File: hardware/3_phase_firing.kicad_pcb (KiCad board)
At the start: 2 copper layers, 90 x 50 mm, 32 parts, among them J1 PHASE_IN_1, J2 PHASE_OUT_1, J3 PHASE_IN_2, J4 PHASE_OUT_2, Q1 BT136-500, Q2 BT136-500, Q3 BT136-500, U1 4N25, U2 4N25, U3 4N25, U4 MEGA_PRO_EMBED_CH340G_{slash}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, U5 MOC3012M, U6 MOC3012M, U7 MOC3012M

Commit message: pcb done
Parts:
- added G***: LOGO, logo_uny:logo_uny_15mm, F.Cu at (153.0, 84.0)
- added REF**: MountingHole_2.5mm_Pad, MountingHole:MountingHole_2.5mm_Pad, F.Cu at (82.0, 125.0)
- added REF**: MountingHole_2.5mm_Pad, MountingHole:MountingHole_2.5mm_Pad, F.Cu at (212.0, 125.0)
- added REF**: MountingHole_2.5mm_Pad, MountingHole:MountingHole_2.5mm_Pad, F.Cu at (212.0, 75.0)
- added REF**: MountingHole_2.5mm_Pad, MountingHole:MountingHole_2.5mm_Pad, F.Cu at (82.0, 75.0)
- U1, U2, U3, U5, U6, U7: footprint Package_DIP:DIP-6_W7.62mm -> Package_DIP:DIP-6_W8.89mm_SMDSocket_LongPads
- U4: moved to B.Cu
- moved U4 155.5 mm to (152.3, 99.0), turned to -90 degrees
- moved R5 106.8 mm to (111.0, 109.0)
- moved R6 106.2 mm to (111.0, 115.0)
- moved U3 79.6 mm to (124.0, 114.3)
- moved J1 67.0 mm to (85.0, 89.9)
- moved J3 67.0 mm to (85.0, 100.5)
- moved R3 58.0 mm to (111.0, 96.0)
- moved R8 56.5 mm to (176.0, 92.0)
- moved U2 54.3 mm to (124.0, 99.0)
- moved Q3 53.6 mm to (200.0, 80.5), turned to -90 degrees
- moved Q2 50.9 mm to (200.0, 96.5), turned to -90 degrees
- moved R7 46.5 mm to (176.0, 77.0)
- moved R15 45.0 mm to (193.0, 87.0)
- moved J2 43.6 mm to (211.0, 106.5)
- moved J4 43.6 mm to (211.0, 95.9)
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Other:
- board size 90 x 50 mm -> 140 x 60 mm
- board text added: "2022 (C) JPTE HFEAA"
- board text added: "MODUL ELDA PEMICU 3 FASA"

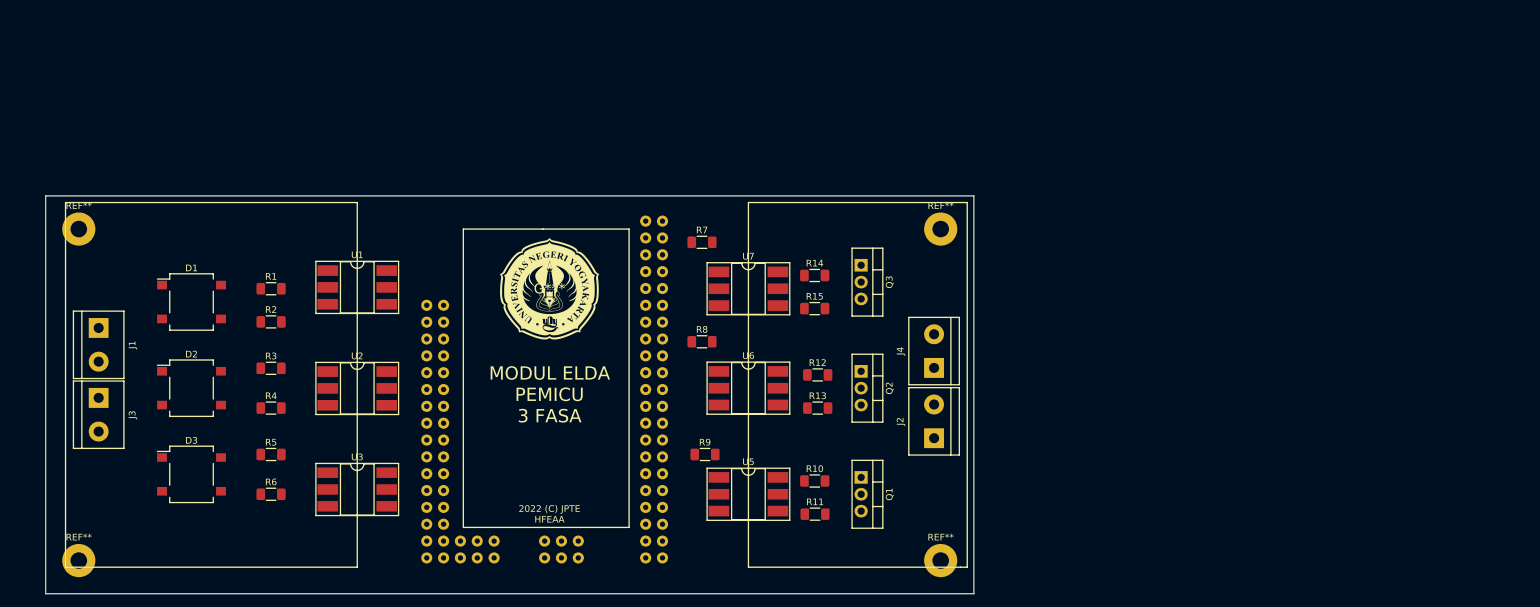
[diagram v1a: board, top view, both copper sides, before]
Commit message: modifying footprint
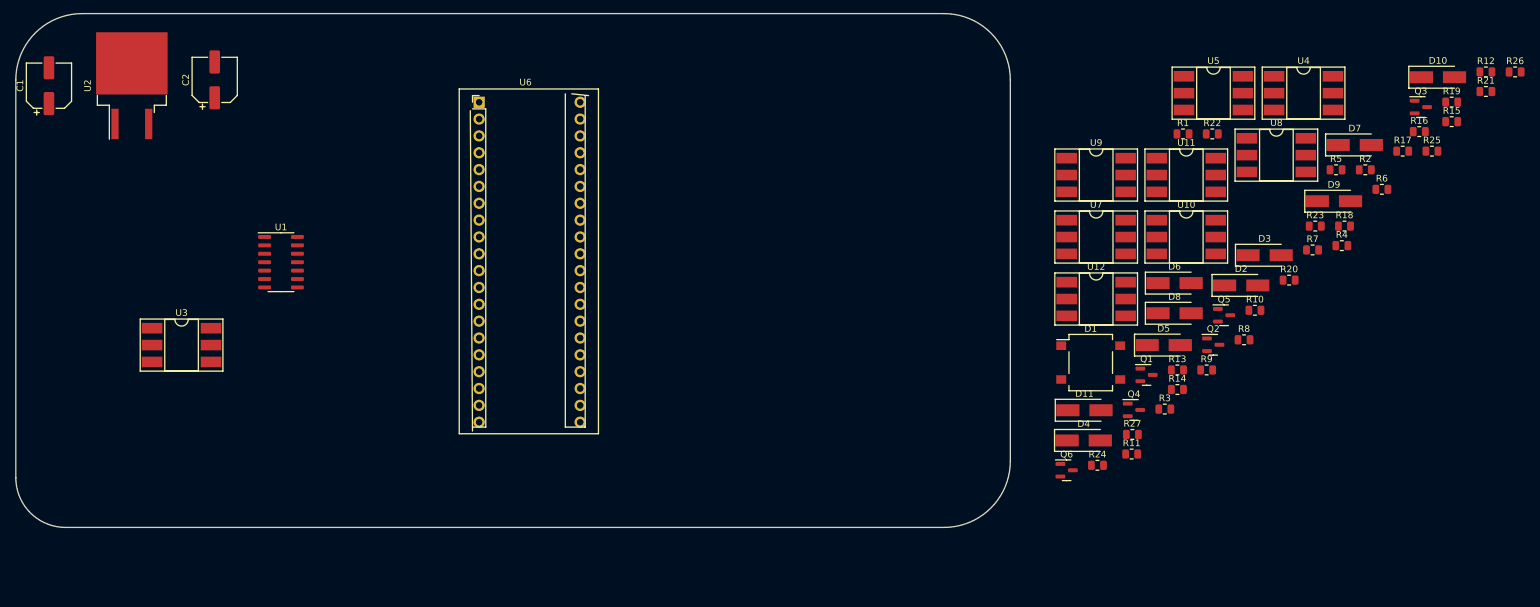
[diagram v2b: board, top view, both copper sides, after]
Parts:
- removed G***: LOGO, logo_uny:logo_uny_15mm
- removed J1: PHASE_IN_1, TerminalBlock:TerminalBlock_bornier-2_P5.08mm
- removed J2: PHASE_OUT_1, TerminalBlock:TerminalBlock_bornier-2_P5.08mm
- removed J3: PHASE_IN_2, TerminalBlock:TerminalBlock_bornier-2_P5.08mm
- removed J4: PHASE_OUT_2, TerminalBlock:TerminalBlock_bornier-2_P5.08mm
- removed REF** (x4): MountingHole_2.5mm_Pad, MountingHole:MountingHole_2.5mm_Pad
- added C1: 100uF, Capacitor_SMD:CP_Elec_6.3x7.7, F.Cu at (77.5, 53.4)
- added C2: 100uF, Capacitor_SMD:CP_Elec_6.3x7.7, F.Cu at (102.5, 52.5)
- added D10: 1N4007, Diode_SMD:D_SMA_Handsoldering, F.Cu at (287.0, 52.1)
- added D11: 1N4007, Diode_SMD:D_SMA_Handsoldering, F.Cu at (233.7, 102.3)
- added D4: 1N4007, Diode_SMD:D_SMA_Handsoldering, F.Cu at (233.6, 106.9)
- added D5: 1N4007, Diode_SMD:D_SMA_Handsoldering, F.Cu at (245.6, 92.5)
- added D6: 1N4007, Diode_SMD:D_SMA_Handsoldering, F.Cu at (247.3, 83.2)
- added D7: 1N4007, Diode_SMD:D_SMA_Handsoldering, F.Cu at (274.4, 62.3)
- added D8: 1N4007, Diode_SMD:D_SMA_Handsoldering, F.Cu at (247.3, 87.7)
- added D9: 1N4007, Diode_SMD:D_SMA_Handsoldering, F.Cu at (271.3, 70.8)
- added Q4: MMBT3904, Package_TO_SOT_SMD:SOT-23, F.Cu at (241.2, 102.3)
- added Q5: MMBT3904, Package_TO_SOT_SMD:SOT-23, F.Cu at (254.7, 88.0)
- added Q6: MMBT3904, Package_TO_SOT_SMD:SOT-23, F.Cu at (231.0, 111.4)
- added R16: 2K2, Resistor_SMD:R_0805_2012Metric, F.Cu at (284.2, 60.3)
- added R17: 2K2, Resistor_SMD:R_0805_2012Metric, F.Cu at (281.7, 63.2)
- added R18: 2K2, Resistor_SMD:R_0805_2012Metric, F.Cu at (272.9, 74.5)
- added R19: 10K, Resistor_SMD:R_0805_2012Metric, F.Cu at (289.1, 55.9)
- added R20: 10K, Resistor_SMD:R_0805_2012Metric, F.Cu at (264.6, 82.7)
- added R21: 10K, Resistor_SMD:R_0805_2012Metric, F.Cu at (294.2, 54.2)
- added R22: 2K2, Resistor_SMD:R_0805_2012Metric, F.Cu at (253.0, 60.6)
- added R23: 2K2, Resistor_SMD:R_0805_2012Metric, F.Cu at (268.5, 74.5)
- added R24: 2K2, Resistor_SMD:R_0805_2012Metric, F.Cu at (235.6, 110.6)
- added R25: 2K2, Resistor_SMD:R_0805_2012Metric, F.Cu at (286.1, 63.2)
- added R26: 2K2, Resistor_SMD:R_0805_2012Metric, F.Cu at (298.6, 51.3)
- added R27: 2K2, Resistor_SMD:R_0805_2012Metric, F.Cu at (240.9, 106.0)
- added U10: 4N35, Package_DIP:DIP-6_W8.89mm_SMDSocket_LongPads, F.Cu at (249.0, 76.2)
- added U11: 4N35, Package_DIP:DIP-6_W8.89mm_SMDSocket_LongPads, F.Cu at (249.0, 66.8)
- added U12: 4N35, Package_DIP:DIP-6_W8.89mm_SMDSocket_LongPads, F.Cu at (235.4, 85.5)
- added U8: 4N35, Package_DIP:DIP-6_W8.89mm_SMDSocket_LongPads, F.Cu at (262.6, 63.9)
- added U9: 4N35, Package_DIP:DIP-6_W8.89mm_SMDSocket_LongPads, F.Cu at (235.4, 66.8)
- D2, D3: value DB106S -> 1N4007; footprint Diode_SMD:Diode_Bridge_OnSemi_SDIP-4L -> Diode_SMD:D_SMA_Handsoldering
- Q1, Q2, Q3: value BT136-500 -> MMBT3904; footprint Package_TO_SOT_THT:TO-220-3_Vertical -> Package_TO_SOT_SMD:SOT-23
- R1, R2, R3, R4, R5, R6: value 2K2 -> 10K; footprint Resistor_SMD:R_1206_3216Metric_Pad1.30x1.75mm_HandSolder -> Resistor_SMD:R_0805_2012Metric
- R10, R12, R13, R14, R15: value 330 -> 10K; footprint Resistor_SMD:R_1206_3216Metric_Pad1.30x1.75mm_HandSolder -> Resistor_SMD:R_0805_2012Metric
- R11: value 330 -> 100K; footprint Resistor_SMD:R_1206_3216Metric_Pad1.30x1.75mm_HandSolder -> Resistor_SMD:R_0805_2012Metric
- R7, R9: value 10K -> 100K; footprint Resistor_SMD:R_1206_3216Metric_Pad1.30x1.75mm_HandSolder -> Resistor_SMD:R_0805_2012Metric
- R8: footprint Resistor_SMD:R_1206_3216Metric_Pad1.30x1.75mm_HandSolder -> Resistor_SMD:R_0805_2012Metric
- U1: value 4N25 -> LM339; footprint Package_DIP:DIP-6_W8.89mm_SMDSocket_LongPads -> Package_SO:SOIC-14_3.9x8.7mm_P1.27mm
- U2: value 4N25 -> L7812; footprint Package_DIP:DIP-6_W8.89mm_SMDSocket_LongPads -> Package_TO_SOT_SMD:TO-263-2
- U3: value 4N25 -> 4N35
- U4: value MEGA_PRO_EMBED_CH340G_/_ATMEGA2560 -> 4N35; footprint MEGA_PRO_EMBED_CH340G___ATMEGA2560:MODULE_MEGA_PRO_EMBED_CH340G___ATMEGA2560 -> Package_DIP:DIP-6_W8.89mm_SMDSocket_LongPads; moved to F.Cu
- U5, U7: value MOC3012M -> 4N35
- U6: value MOC3012M -> YAAJ_WeAct_BlackPill_Part_Like; footprint Package_DIP:DIP-6_W8.89mm_SMDSocket_LongPads -> Footprints:YAAJ_WeAct_BlackPill_2
- moved R6 173.7 mm to (278.5, 69.0)
- moved R2 166.6 mm to (276.0, 66.1)
- moved R5 166.3 mm to (271.6, 66.1)
- moved D3 165.2 mm to (260.9, 79.0)
- moved R4 163.3 mm to (272.5, 77.5)
- moved D2 159.1 mm to (257.3, 83.5)
- moved R1 139.5 mm to (248.6, 60.6)
- moved D1 135.9 mm to (234.6, 95.1)
- moved R3 134.9 mm to (245.8, 102.2)
- moved U4 122.8 mm to (266.7, 54.5), turned to 0 degrees
- moved R12 110.7 mm to (294.2, 51.3)
- moved R15 100.1 mm to (289.1, 58.8)
- moved U5 92.6 mm to (253.1, 54.5)
- moved R7 92.1 mm to (268.1, 78.2)
- moved Q3 87.7 mm to (284.4, 56.6), turned to 0 degrees
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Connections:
- D1 pad 1: Net-(D1-Pad1) -> GNDS
- D1 pad 2: N -> PHASE_A
- D1 pad 4: PHASE_A -> NEUT
- D2 pad 2: N -> PHASE_A
- D3 pad 2: N -> PHASE_B
- Q1 pad 1: OUT_A -> TRIAC_MODE
- Q1 pad 2: PHASE_A -> Net-(Q1-Pad2)
- Q2 pad 1: OUT_B -> TRIAC_MODE
- Q2 pad 2: PHASE_B -> Net-(Q2-Pad2)
- Q3 pad 1: OUT_C -> TRIAC_MODE
- Q3 pad 2: PHASE_C -> Net-(Q3-Pad2)
- R1 pad 1: Net-(D1-Pad1) -> Net-(R1-Pad1)
- R1 pad 2: Net-(R1-Pad2) -> Net-(D2-Pad1)
- R10 pad 1: Net-(R10-Pad1) -> GNDS
- R10 pad 2: PHASE_A -> Net-(R10-Pad2)
- R11 pad 2: Net-(Q1-Pad3) -> VCC
- R12 pad 1: Net-(R12-Pad1) -> GNDS
- R12 pad 2: PHASE_B -> Net-(R11-Pad1)
- R13 pad 2: Net-(Q2-Pad3) -> VCC
- R14 pad 2: PHASE_C -> VCC
- R15 pad 2: Net-(Q3-Pad3) -> VCC
- R2 pad 1: Net-(D1-Pad3) -> GNDS
- R2 pad 2: Net-(R2-Pad2) -> Net-(R1-Pad1)
- R3 pad 1: Net-(D2-Pad1) -> Net-(R3-Pad1)
- R3 pad 2: Net-(R3-Pad2) -> Net-(D3-Pad1)
- R4 pad 1: Net-(D2-Pad3) -> GNDS
- R4 pad 2: Net-(R4-Pad2) -> Net-(R3-Pad1)
- R5 pad 1: Net-(D3-Pad1) -> Net-(R5-Pad1)
- R5 pad 2: Net-(R5-Pad2) -> Net-(D4-Pad1)
- R6 pad 1: Net-(D3-Pad3) -> GNDS
- R6 pad 2: Net-(R6-Pad2) -> Net-(R5-Pad1)
- R7 pad 1: +5V -> Net-(R7-Pad1)
- R7 pad 2: A_ZERO_CROSS -> VCC
- R8 pad 1: +5V -> GNDS
- R8 pad 2: B_ZERO_CROSS -> Net-(R7-Pad1)
- R9 pad 1: +5V -> Net-(R10-Pad2)
- R9 pad 2: C_ZERO_CROSS -> VCC
- U1 pad 1: Net-(R1-Pad2) -> Net-(R14-Pad1)
- U1 pad 2: Net-(R2-Pad2) -> Net-(R13-Pad1)
- U1 pad 3: unconnected-(U1-Pad3) -> Net-(C2-Pad1)
- U1 pad 4: GND -> Net-(R7-Pad1)
- U1 pad 5: A_ZERO_CROSS -> Net-(R1-Pad1)
- U1 pad 6: unconnected-(U1-Pad6) -> Net-(R10-Pad2)
- U2 pad 1: Net-(R3-Pad2) -> Net-(C1-Pad1)
- U2 pad 2: Net-(R4-Pad2) -> GNDS
- U2 pad 3: unconnected-(U2-Pad3) -> Net-(C2-Pad1)
- U3 pad 1: Net-(R5-Pad2) -> Net-(R16-Pad1)
- U3 pad 2: Net-(R6-Pad2) -> GNDS
- U3 pad 5: C_ZERO_CROSS -> ZCD_A
- U5 pad 1: A_TRIGGER -> Net-(R18-Pad1)
- U5 pad 2: GND -> GNDS
- U5 pad 4: Net-(R11-Pad1) -> GND
- U5 pad 5: unconnected-(U5-Pad5) -> ZCD_C
- U5 pad 6: Net-(R10-Pad1) -> unconnected-(U5-Pad6)
- U6 pad 1: B_TRIGGER -> unconnected-(U6-Pad1)
- U6 pad 2: GND -> unconnected-(U6-Pad2)
- U6 pad 4: Net-(R13-Pad1) -> unconnected-(U6-Pad4)
- U6 pad 6: Net-(R12-Pad1) -> unconnected-(U6-Pad6)
- U7 pad 1: C_TRIGGER -> Net-(R22-Pad1)
- U7 pad 4: Net-(R15-Pad1) -> OUTB1_E
- U7 pad 5: unconnected-(U7-Pad5) -> OUTB1_C
- U7 pad 6: Net-(R14-Pad1) -> unconnected-(U7-Pad6)
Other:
- board size 140 x 60 mm -> 150 x 77.5 mm
- board text removed: "2022 (C) JPTE HFEAA"
- board text removed: "MODUL ELDA PEMICU 3 FASA"

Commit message: done with pcb layouting, routing need to done more
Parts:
- added J1: IN1, TerminalBlock:TerminalBlock_bornier-2_P5.08mm, F.Cu at (77.5, 67.5)
- added J2: IN2, TerminalBlock:TerminalBlock_bornier-2_P5.08mm, F.Cu at (77.5, 92.5)
- added J3: OUT, TerminalBlock_Phoenix:TerminalBlock_Phoenix_MKDS-3-12-5.08_1x12_P5.08mm_Horizontal, F.Cu at (207.8, 110.4)
- D11, D7, D9, Q4, Q5, Q6, R23, R25, R27, U10, U12, U8: moved to B.Cu
- moved R12 191.0 mm to (107.3, 90.7), turned to 90 degrees
- moved R2 188.5 mm to (88.4, 84.3), turned to 90 degrees
- moved R6 185.4 mm to (96.0, 101.8), turned to 90 degrees
- moved R15 179.5 mm to (111.3, 83.6), turned to 90 degrees
- moved R5 179.4 mm to (95.0, 97.5), turned to 180 degrees
- moved D2 177.4 mm to (80.0, 80.0), turned to 180 degrees
- moved D3 173.9 mm to (87.5, 92.5), turned to 180 degrees
- moved R4 173.7 mm to (99.5, 92.5), turned to 180 degrees
- moved R7 172.6 mm to (95.5, 78.7), turned to 180 degrees
- moved R16 170.2 mm to (114.0, 64.8), turned to 180 degrees
- moved R17 168.5 mm to (113.8, 77.5), turned to 180 degrees
- moved R21 166.8 mm to (132.1, 93.3), turned to -90 degrees
- moved D5 165.3 mm to (83.6, 59.9), turned to -90 degrees
- moved R10 163.9 mm to (95.5, 85.3)
- moved R8 162.6 mm to (95.5, 81.0)
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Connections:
- C2 pad 1: Net-(C2-Pad1) -> VCC
- U1 pad 3: Net-(C2-Pad1) -> VCC
- U2 pad 3: Net-(C2-Pad1) -> VCC
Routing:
- net GNDS: track 0.00 -> 85.3 mm, vias 0 -> 22
- net PHASE_A: track 0.00 -> 33.3 mm
- net Net-(R13-Pad1): track 0.00 -> 29.9 mm
- net Net-(R5-Pad1): track 0.00 -> 25.4 mm
- net Net-(C1-Pad1): track 0.00 -> 19.9 mm
- net Net-(R14-Pad1): track 0.00 -> 18.4 mm
- net Net-(R1-Pad1): track 0.00 -> 15.8 mm
- net VCC: track 0.00 -> 10.9 mm
- net Net-(R3-Pad1): track 0.00 -> 10.7 mm
- net Net-(R11-Pad1): track 0.00 -> 10.5 mm
- net NEUT: track 0.00 -> 10.3 mm
- net Net-(R15-Pad1): track 0.00 -> 10.3 mm
- net PHASE_C: track 0.00 -> 7.53 mm
- net PHASE_B: track 0.00 -> 7.50 mm
- net Net-(R18-Pad1): track 0.00 -> 7.18 mm
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- added copper zone on B.Cu, net GNDS
- added copper zone on F.Cu, net VCC
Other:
- board size 150 x 77.5 mm -> 142.5 x 77.5 mm

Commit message: fixing kicad_pcb files
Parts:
- removed Q4, Q5, Q6: MMBT3904, Package_TO_SOT_SMD:SOT-23
- added G***: LOGO, logo_uny:logo_uny_15mm, F.Cu at (86.4, 109.5)
- added J4: USB_LED, Connector_JST:JST_XH_B2B-XH-A_1x02_P2.50mm_Vertical, F.Cu at (170.2, 114.3)
- added J5: POWER, Connector_JST:JST_XH_B2B-XH-A_1x02_P2.50mm_Vertical, F.Cu at (180.3, 114.3)
- added R28: 220, Resistor_SMD:R_0805_2012Metric, F.Cu at (170.2, 108.0)
- added R29: 220, Resistor_SMD:R_0805_2012Metric, F.Cu at (180.3, 108.0)
- added REF**: MountingHole_3.2mm_M3_DIN965_Pad, MountingHole:MountingHole_3.2mm_M3_DIN965_Pad, F.Cu at (195.0, 113.0)
- added REF**: MountingHole_3.2mm_M3_DIN965_Pad, MountingHole:MountingHole_3.2mm_M3_DIN965_Pad, F.Cu at (80.0, 51.3)
- added REF**: MountingHole_3.2mm_M3_DIN965_Pad, MountingHole:MountingHole_3.2mm_M3_DIN965_Pad, F.Cu at (195.0, 51.0)
- moved R23 5.67 mm to (176.2, 81.3), turned to 180 degrees
- moved D11 2.57 mm to (166.9, 97.9)
- moved D6 2.57 mm to (166.6, 76.1)
- moved D7 2.57 mm to (166.7, 81.4)
- moved D8 2.57 mm to (166.6, 60.1)
- moved Q2 2.57 mm to (171.4, 65.4)
- moved D10 2.57 mm to (166.6, 91.8)
- moved D9 2.57 mm to (166.4, 65.2)
- moved Q1 2.57 mm to (170.9, 81.4)
- moved Q3 2.57 mm to (170.9, 98.9)
- moved R25 1.27 mm to (176.5, 64.8), turned to 180 degrees
- moved R24 1.12 mm to (176.2, 59.7), turned to 180 degrees
- moved R26 0.74 mm to (177.2, 91.4)
- moved R27 0.28 mm to (176.8, 97.5)
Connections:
- U6 pad 14: unconnected-(U6-Pad14) -> ZCD_C
- U6 pad 15: unconnected-(U6-Pad15) -> GATE_C1
- U6 pad 16: unconnected-(U6-Pad16) -> GATE_C2
- U6 pad 2: unconnected-(U6-Pad2) -> LED_USB
- U6 pad 32: unconnected-(U6-Pad32) -> ZCD_B
- U6 pad 33: unconnected-(U6-Pad33) -> GATE_B1
- U6 pad 34: unconnected-(U6-Pad34) -> GATE_B2
- U6 pad 4: unconnected-(U6-Pad4) -> TRIAC_MODE
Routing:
- net TRIAC_MODE: track 0.00 -> 110.2 mm, vias 0 -> 6
- net ZCD_A: track 0.00 -> 81.9 mm, vias 0 -> 2
- net ZCD_B: track 0.00 -> 79.7 mm, vias 0 -> 2
- net LED_USB: track 0.00 -> 74.1 mm, vias 0 -> 1
- net GATE_C1: track 0.00 -> 54.0 mm, vias 0 -> 1
- net GATE_C2: track 0.00 -> 46.3 mm
- net GATE_A1: track 0.00 -> 35.2 mm
- net OUTC2_C: track 0.00 -> 30.9 mm, vias 0 -> 1
- net OUTB2_C: track 0.00 -> 30.6 mm, vias 0 -> 1
- net OUTA2_C: track 0.00 -> 30.4 mm, vias 0 -> 1
- net OUTC2_E: track 0.00 -> 29.4 mm
- net GATE_A2: track 0.00 -> 28.7 mm, vias 0 -> 2
- net OUTB2_E: track 0.00 -> 25.2 mm
- net OUTA2_E: track 0.00 -> 24.5 mm
- net Net-(D10-Pad1): track 0.00 -> 19.8 mm
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- added copper zone on F.Cu, net +3.3V
- added copper zone on B.Cu, net GND
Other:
- board text added: "!!!HIGH VOLTAGE!!!"
- board text added: "A"
- board text added: "B"
- board text added: "C"
- board text added: "DESIGN : HILAL YAHYA SUPERVISOR :"
- board text added: "HW-ID : ACRC-01 REV NUM : v0.2"
- board text added: "ISOLATED"
- board text added: "MODUL PEMICU AC REGULATOR & DC KONVERTER"
- board text added: "N"

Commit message: Revert "tracing path of the pcb"
This reverts commit a1f78cd755137d86b9aab8dfdd90e54233a75f74.
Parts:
- removed G***: LOGO, logo_uny:logo_uny_15mm
- removed J4: USB_LED, Connector_JST:JST_XH_B2B-XH-A_1x02_P2.50mm_Vertical
- removed J5: POWER, Connector_JST:JST_XH_B2B-XH-A_1x02_P2.50mm_Vertical
- removed R28, R29: 220, Resistor_SMD:R_0805_2012Metric
- removed REF** (x3): MountingHole_3.2mm_M3_DIN965_Pad, MountingHole:MountingHole_3.2mm_M3_DIN965_Pad
- added Q4: MMBT3904, Package_TO_SOT_SMD:SOT-23, B.Cu at (169.4, 74.4)
- added Q5: MMBT3904, Package_TO_SOT_SMD:SOT-23, B.Cu at (168.9, 58.2)
- added Q6: MMBT3904, Package_TO_SOT_SMD:SOT-23, B.Cu at (170.4, 89.7)
- moved R23 5.67 mm to (177.1, 75.7), turned to 0 degrees
- moved D11 2.57 mm to (169.4, 97.5)
- moved D6 2.57 mm to (169.1, 75.7)
- moved D7 2.57 mm to (169.2, 81.0)
- moved D8 2.57 mm to (169.1, 59.7)
- moved Q2 2.57 mm to (174.0, 65.0)
- moved D10 2.57 mm to (169.2, 91.4)
- moved D9 2.57 mm to (168.9, 64.8)
- moved Q1 2.57 mm to (173.5, 81.0)
- moved Q3 2.57 mm to (173.5, 98.6)
- moved R25 1.27 mm to (177.8, 64.8), turned to 0 degrees
- moved R24 1.12 mm to (177.3, 59.7), turned to 0 degrees
- moved R26 0.74 mm to (177.9, 91.4)
- moved R27 0.28 mm to (176.5, 97.5)
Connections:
- U6 pad 14: ZCD_C -> unconnected-(U6-Pad14)
- U6 pad 15: GATE_C1 -> unconnected-(U6-Pad15)
- U6 pad 16: GATE_C2 -> unconnected-(U6-Pad16)
- U6 pad 2: LED_USB -> unconnected-(U6-Pad2)
- U6 pad 32: ZCD_B -> unconnected-(U6-Pad32)
- U6 pad 33: GATE_B1 -> unconnected-(U6-Pad33)
- U6 pad 34: GATE_B2 -> unconnected-(U6-Pad34)
- U6 pad 4: TRIAC_MODE -> unconnected-(U6-Pad4)
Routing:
- net TRIAC_MODE: track 110.2 -> 0.00 mm, vias 6 -> 0
- net ZCD_A: track 81.9 -> 0.00 mm, vias 2 -> 0
- net ZCD_B: track 79.7 -> 0.00 mm, vias 2 -> 0
- net LED_USB: track 74.1 -> 0.00 mm, vias 1 -> 0
- net GATE_C1: track 54.0 -> 0.00 mm, vias 1 -> 0
- net GATE_C2: track 46.3 -> 0.00 mm
- net GATE_A1: track 35.2 -> 0.00 mm
- net OUTC2_C: track 30.9 -> 0.00 mm, vias 1 -> 0
- net OUTB2_C: track 30.6 -> 0.00 mm, vias 1 -> 0
- net OUTA2_C: track 30.4 -> 0.00 mm, vias 1 -> 0
- net OUTC2_E: track 29.4 -> 0.00 mm
- net GATE_A2: track 28.7 -> 0.00 mm, vias 2 -> 0
- net OUTB2_E: track 25.2 -> 0.00 mm
- net OUTA2_E: track 24.5 -> 0.00 mm
- net Net-(D10-Pad1): track 19.8 -> 0.00 mm
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- removed copper zone on F.Cu, net +3.3V
- removed copper zone on B.Cu, net GND
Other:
- board text removed: "!!!HIGH VOLTAGE!!!"
- board text removed: "A"
- board text removed: "B"
- board text removed: "C"
- board text removed: "DESIGN : HILAL YAHYA SUPERVISOR :"
- board text removed: "HW-ID : ACRC-01 REV NUM : v0.2"
- board text removed: "ISOLATED"
- board text removed: "MODUL PEMICU AC REGULATOR & DC KONVERTER"
- board text removed: "N"
